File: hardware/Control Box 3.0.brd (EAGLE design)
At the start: 99.1 x 69.8 mm, 27 parts, among them IC1 LM324N, J1 AC_IN, J2 To_Relay, J3 From_Relay, J4 AC_OUT, J5 To_Reg, J6 From_Reg, J7 54601-908WPLFW/MODEL, K1 T9AS1D22-54PIN, K2 T9AS1D22-54PIN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

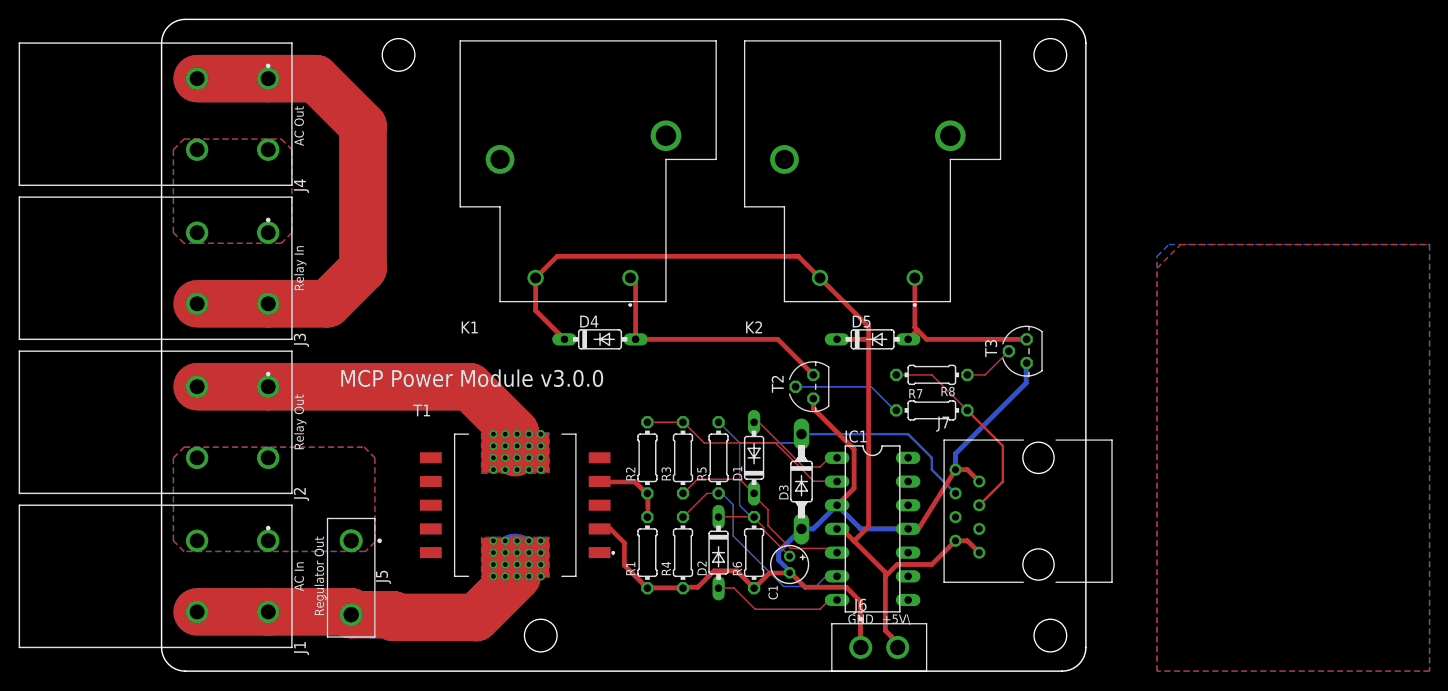
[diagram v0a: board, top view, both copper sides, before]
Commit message: Replace LM324 with LM358, clean up component names, silkscreen layout, and some routing
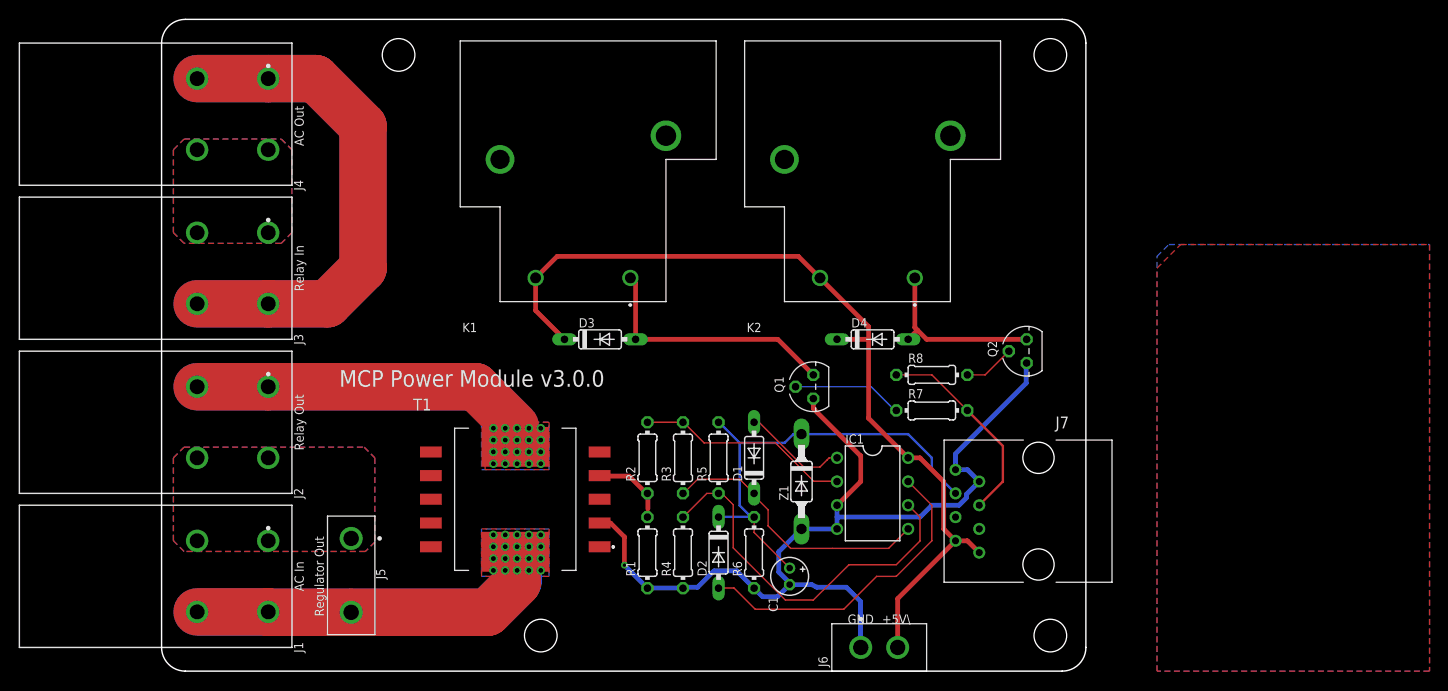
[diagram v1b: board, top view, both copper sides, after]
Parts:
- removed D5: 1N4148, diode:DO35-7
- added Z1: BZD23, diode:SOD81
- D3: value BZD23 -> 1N4148; device diode:SOD81 -> diode:DO35-7
- IC1: value LM324N -> LM358N; device mcp:DIL14 -> linear:DIL08
- moved D4 29.2 mm to (76.2, 35.6)
- moved D3 26.4 mm to (47.0, 35.6), turned to 0 degrees
- moved IC1 3.81 mm to (76.2, 19.1)
- moved C1 1.27 mm to (67.3, 10.2)
- moved T1 0.63 mm to (38.1, 18.4)
- moved J5 0.25 mm to (20.3, 14.2)
- renumbered T2 to Q1, T3 to Q2
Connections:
- net +5V: now also D3.C, IC1.8; no longer D5.C, IC1.4
- net CURRENT_OUT: now also Z1.C; no longer D3.C
- net GND: now also IC1.4, Z1.A; no longer D3.A, IC1.11
- net N$11: now also D4.A; no longer D5.A
- net N$8: now also D3.A; no longer D4.A
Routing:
- net N$9: track 14.1 -> 34.3 mm
- net N$6: track 24.1 -> 40.9 mm
- net N$5: track 21.6 -> 29.9 mm
- net +5V: track 102.5 -> 95.6 mm
- net AC1: track 80.7 -> 76.4 mm
- net GND: track 100.5 -> 103.8 mm, vias 0 -> 1
- net AC1': track 74.4 -> 71.7 mm
- net CURRENT_OUT: track 48.9 -> 49.4 mm
- added copper zone on layer 1, net AC1'
- added copper zone on layer 1, net AC1
